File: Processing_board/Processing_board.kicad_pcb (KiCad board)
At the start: 4 copper layers, 95.2 x 62 mm, 146 parts, among them J1 Conn_01x08_Pin, J10 CONMHF1-SMD-G-T, J11 USB4215-03-A_REVA, J12 Conn_01x02_Pin, J2 Conn_01x08_Pin, J3 Conn_01x06_Pin, J4 Conn_01x03_Pin, J5 Conn_01x03_Pin, J6 Conn_01x02_Pin, J8 Conn_01x03_Pin, J9 Conn_01x03_Pin, Q1 DMP3056LSS-13, Q2 DMN66D0LT-7, Q3 DMN66D0LT-7, SW1 TL3305BF100QG, SW2 TL3305BF100QG, U1 STM32WBA63CIU6, U10 ADS1299IPAG, U11 ADS1299IPAG, U5 LD1117S50TR_SOT223, U6 LD1117S33TR_SOT223, U8 BGS13SN8E6327XTSA1, U9 MCP2200-I_SO

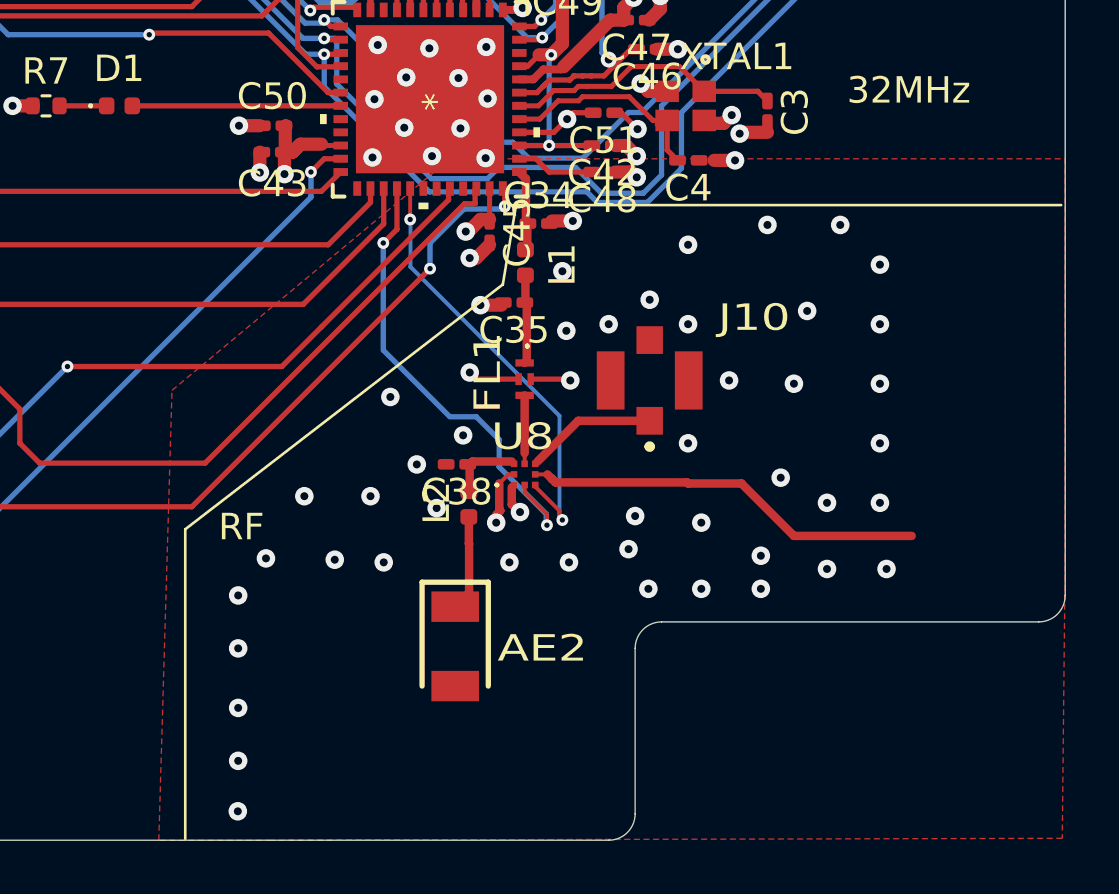
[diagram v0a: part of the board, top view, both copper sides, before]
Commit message: RF_circuit schematic updated and board adapted
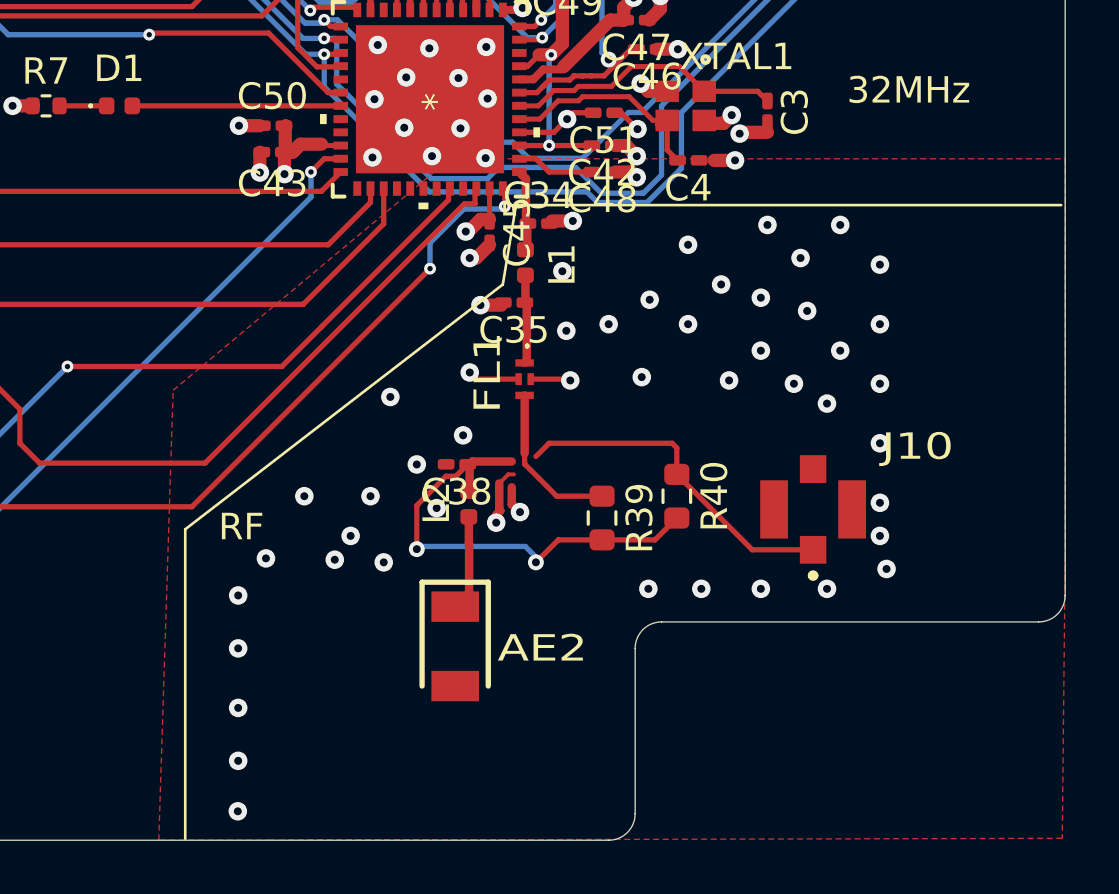
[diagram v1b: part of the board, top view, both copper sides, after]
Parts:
- removed U8: BGS13SN8E6327XTSA1, BGS13SN8E6327XTSA1:BGS13SN8E6327XTSA1
- added R39: 0, Resistor_SMD:R_0603_1608Metric, F.Cu at (156.5, 115.8)
- added R40: 0, Resistor_SMD:R_0603_1608Metric, F.Cu at (159.3, 115.0)
- moved J10 7.87 mm to (164.5, 115.5)
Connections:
- AE2 pad 2: unconnected-(AE2-NC-Pad2) -> GND
- J10 pad 1: /RF circuitry & antennas/RF_UFL_ANT -> Net-(J10-Pad1)
- U1 pad 28: /ANT_LOGIC_2 -> unconnected-(U1-PA12-Pad28)
- U1 pad 29: /ANT_LOGIC_1 -> unconnected-(U1-PA11-Pad29)
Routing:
- net /ANT_LOGIC_2: track 17.9 -> 0.00 mm, vias 2 -> 0
- net /ANT_LOGIC_1: track 16.6 -> 0.00 mm, vias 2 -> 0
- net /RF circuitry & antennas/RF_PCB_ANT: track 15.2 -> 0.00 mm
- net /RF circuitry & antennas/RF_CERAMIC_MATCH: track 2.66 -> 17.8 mm, vias 0 -> 2
- net Net-(J10-Pad1): track 0.00 -> 12.9 mm
- net /RF circuitry & antennas/RF_UFL_ANT: track 4.88 -> 0.00 mm
- net /RF circuitry & antennas/RF_LPF: track 2.59 -> 6.30 mm
